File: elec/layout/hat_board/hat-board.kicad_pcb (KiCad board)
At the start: 4 copper layers, 108 x 115.9 mm, 82 parts, among them P1 HatButtonAntenna, U1 _NXP_Semicon_PN5321A3HN_C106_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, U10 _OPSCO_Optoelectronics_SK6805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, U11 _OPSCO_Optoelectronics_SK6805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, U12 _OPSCO_Optoelectronics_SK6805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, U13 _OPSCO_Optoelectronics_SK6805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, U14 _OPSCO_Optoelectronics_SK6805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, U15 _OPSCO_Optoelectronics_SK6805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, U16 _OPSCO_Optoelectronics_SK6805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, U17 _OPSCO_Optoelectronics_SK6805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, U18 _OPSCO_Optoelectronics_SK6805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, U19 _OPSCO_Optoelectronics_SK6805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, U2 _OPSCO_Optoelectronics_SK6805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, U20 _OPSCO_Optoelectronics_SK6805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, U21 _OPSCO_Optoelectronics_SK6805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, U22 _OPSCO_Optoelectronics_SK6805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, U23 _OPSCO_Optoelectronics_SK6805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, U24 _OPSCO_Optoelectronics_SK6805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, U25 _Microchip_Tech_CAP1188_1_CP_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, U3 _OPSCO_Optoelectronics_SK6805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, U4 _OPSCO_Optoelectronics_SK6805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, U5 _OPSCO_Optoelectronics_SK6805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, U6 _OPSCO_Optoelectronics_SK6805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, U7 _OPSCO_Optoelectronics_SK6805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, U8 _OPSCO_Optoelectronics_SK6805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, U9 _OPSCO_Optoelectronics_SK6805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

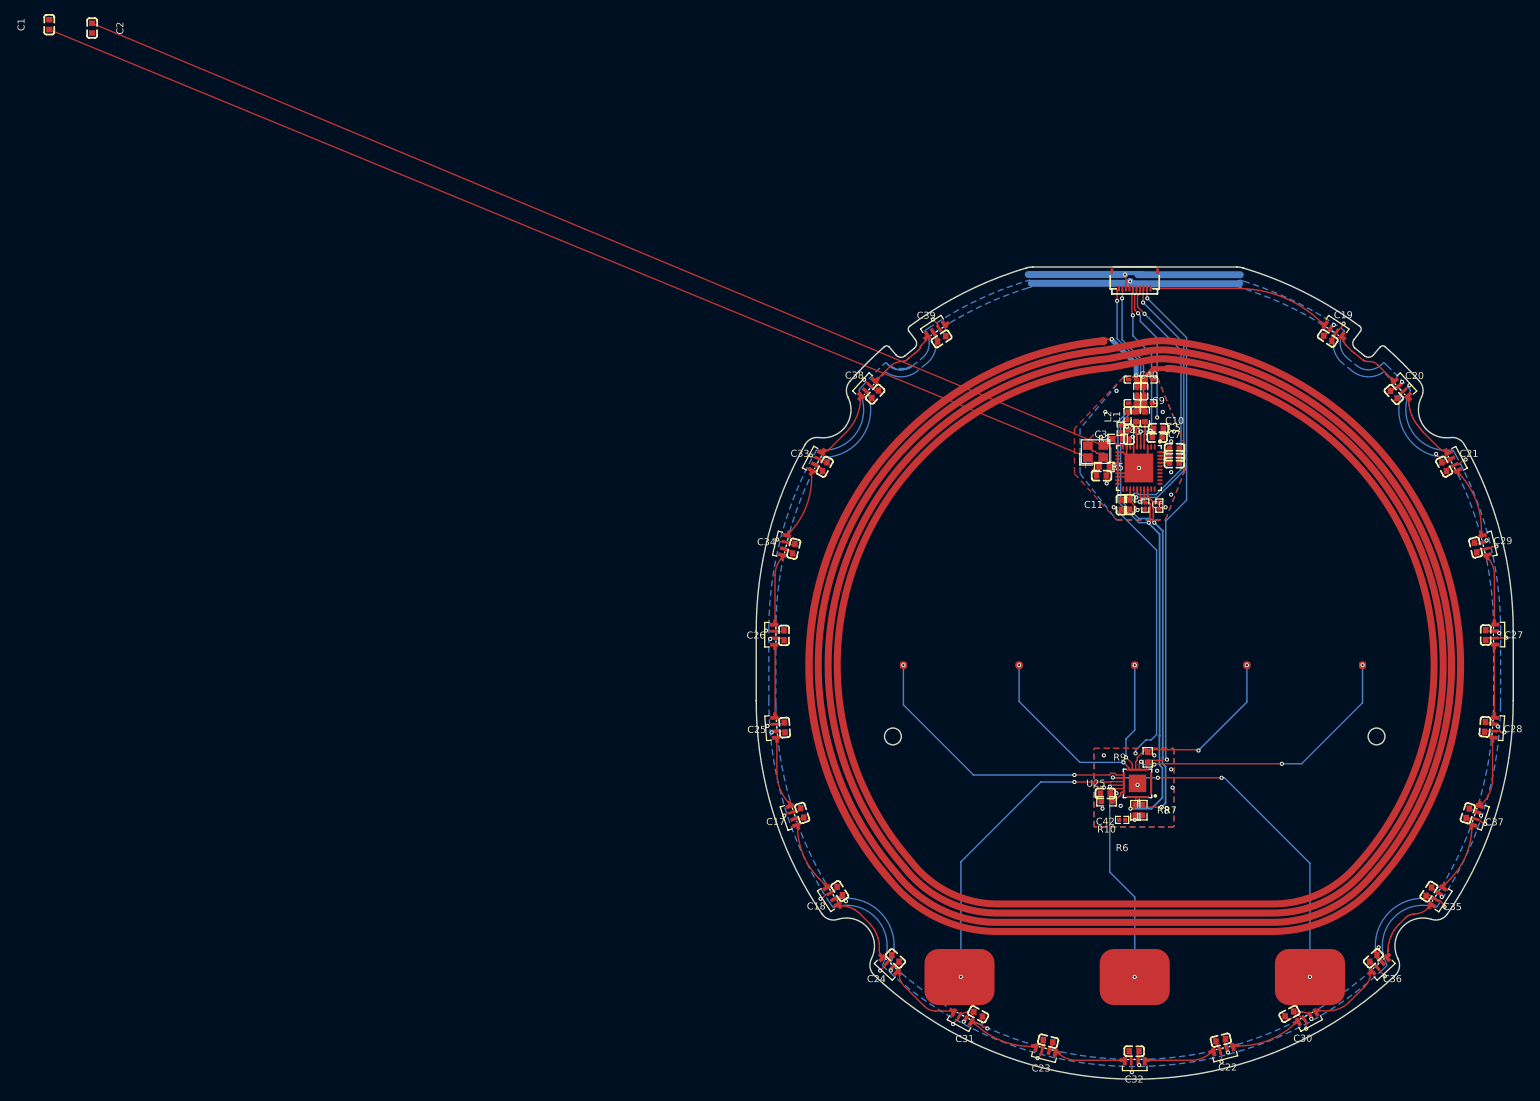
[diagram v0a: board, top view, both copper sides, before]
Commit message: Don't update PCB files
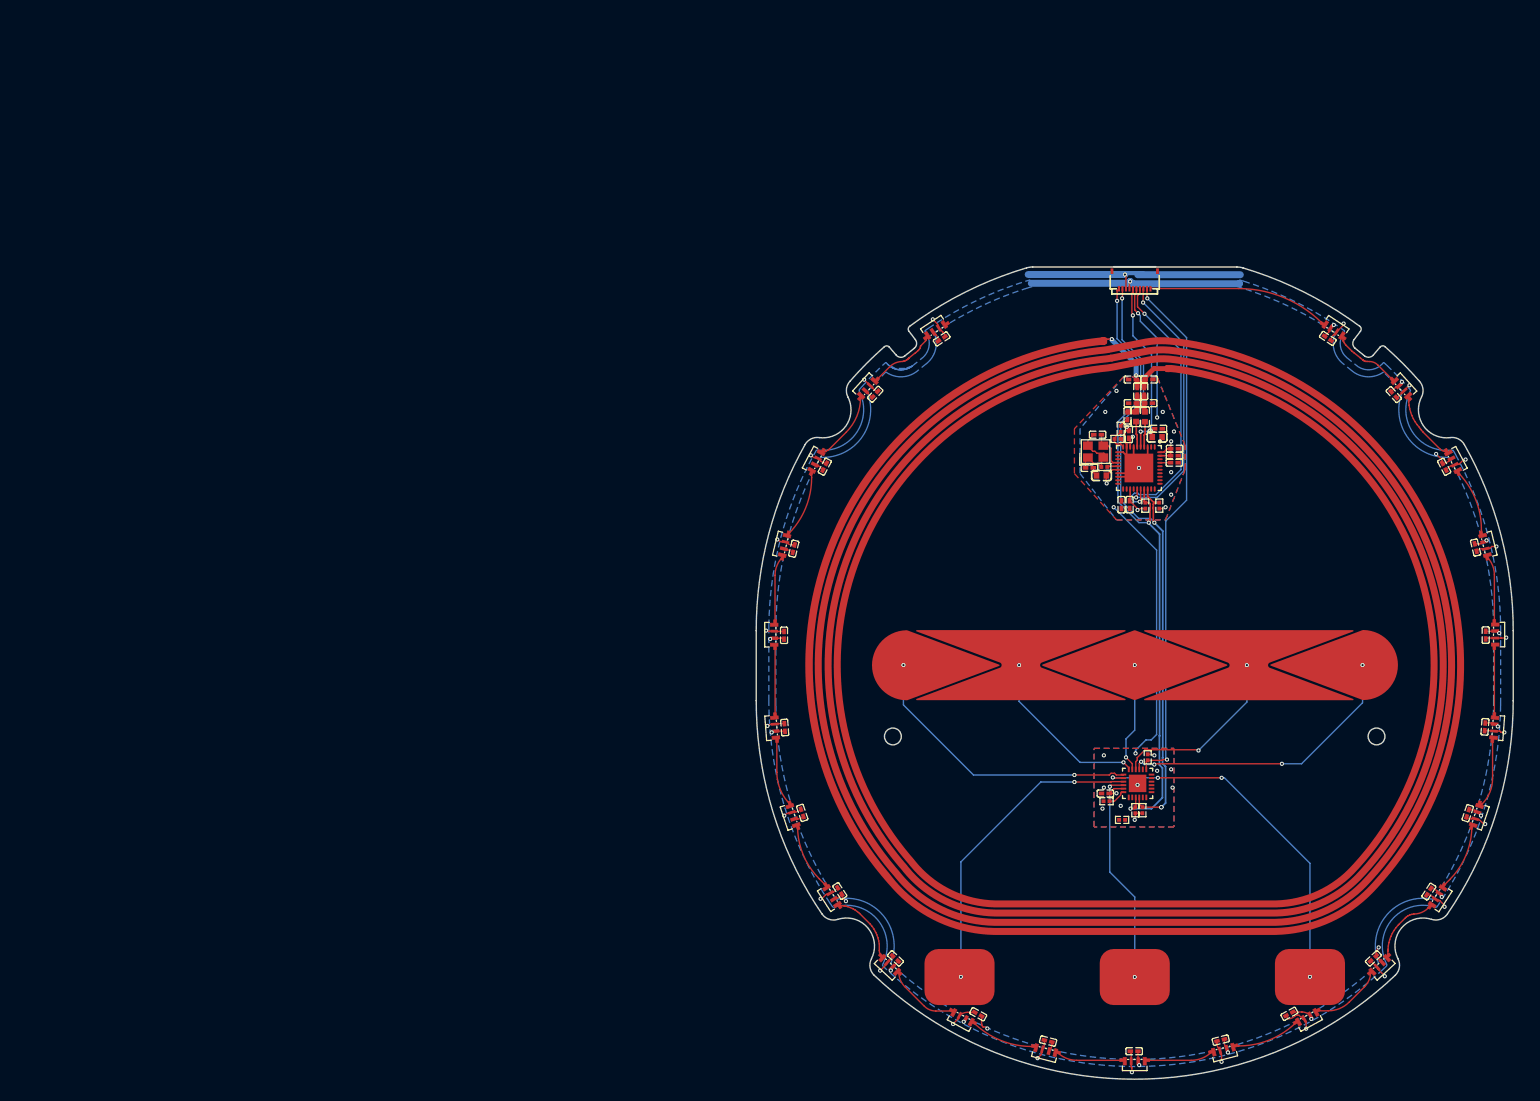
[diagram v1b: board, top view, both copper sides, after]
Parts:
- C1, C2: value 100nF ±10% 50V X7R -> 20pF ±5% 50V C0G; footprint lcsc:C0603 -> lcsc:C0402
- C10, C11, C17, C18, C19, C20, C21, C22, C23, C24, C25, C26, C27, C28, C29, C3, C30, C31, C32, C33, C34, C35, C36, C37, C38, C39, C42, C5, C6, C7, C9: value 100nF ±10% 50V X7R -> 100nF ±10% 16V X7R; footprint lcsc:C0603 -> lcsc:C0402
- C4, C8: value 100nF ±10% 50V X7R -> 10µF ±10% 10V X5R
- L1, L2: value 560nH ±5% infHz 450mA 480mΩ -> 560nH ±5% 450mA 480mΩ
- R1, R2: value 10kΩ ±1% 62.5mW -> 5.1kΩ ±1% 62.5mW
- R10, R9: value 1kΩ ±1% 100mW -> 10kΩ ±1% 62.5mW; footprint lcsc:R0603 -> lcsc:R0402
- R3, R5, R7, R8: value 1kΩ ±1% 100mW -> 5.1kΩ ±1% 62.5mW; footprint lcsc:R0603 -> lcsc:R0402
- U25: footprint lcsc:QFN-24_L4.0-W4.0-P0.50-BL-EP2.5 -> lcsc:QFN-24_L4.0-W4.0-P0.50-TL-EP2.5
- moved C1 161.3 mm to (145.3, 63.0), turned to 0 degrees
- moved C2 154.7 mm to (146.5, 58.2), turned to 180 degrees
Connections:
- C10 pad 1: power_5v -> power_3v3
- C11 pad 1: power_5v -> gnd
- C11 pad 2: gnd -> lv
- C12 pad 2: nfc-net-6 -> nfc-net
- C2 pad 1: nfc-net -> nfc-net-3
- C32 pad 1: power_3v3 -> power_5v
- C33 pad 1: power_3v3 -> power_5v
- C34 pad 1: power_3v3 -> power_5v
- C35 pad 1: power_3v3 -> power_5v
- C36 pad 1: nfc-net-2 -> power_5v
- C37 pad 1: power_3v3 -> power_5v
- C38 pad 1: power_3v3 -> power_5v
- C39 pad 1: power_3v3 -> power_5v
- C4 pad 1: power_5v -> power_3v3
- C42 pad 1: gnd -> power_3v3
- C42 pad 2: lv -> gnd
- C5 pad 1: power_5v -> power_3v3
- C6 pad 1: power_5v -> power_3v3
- C7 pad 1: power_5v -> nfc-net-4
- C8 pad 1: power_5v -> power_3v3
- C9 pad 1: power_5v -> power_3v3
- L1 pad 2: nfc-net-1 -> nfc-net-2
- R1 pad 1: capacitive_sensor-net-1 -> i2c_scl
- R1 pad 2: gnd -> power_3v3
- R10 pad 1: i2c_sda -> capacitive_sensor-net
- R10 pad 2: power_3v3 -> gnd
- R2 pad 1: capacitive_sensor-net -> i2c_sda
- R2 pad 2: gnd -> power_3v3
- R3 pad 2: nfc-net-3 -> nfc-net-6
- R4 pad 1: nfc-net-6 -> nfc-net
- R4 pad 2: nfc-net-4 -> nfc-net-1
- R5 pad 2: nfc-net-4 -> nfc-net-1
- R6 pad 1: touch_irq -> capacitive_sensor.address-signal
- R6 pad 2: power_3v3 -> gnd
- R9 pad 1: i2c_scl -> touch_irq
- U1 pad 10: nfc-net-4 -> nfc-net-1
- U1 pad 14: nfc-net -> nfc-net-3
- U1 pad 15: nfc-net-3 -> nfc-net-6
- U1 pad 20: nfc.nfc_ic.footprint.pins[12].net-net -> nfc.nfc_ic-net
- U1 pad 21: nfc.nfc_ic.footprint.pins[13].net-net -> nfc.nfc_ic-net
- U1 pad 22: nfc.nfc_ic.footprint.pins[14].net-net -> nfc.nfc_ic-net
- U1 pad 37: nfc-net-2 -> nfc-net-4
- U1 pad 4: nfc-net-1 -> nfc-net-2
- U10 pad 1: signal-17 -> signal-1
- U10 pad 4: signal-19 -> signal-16
- U11 pad 1: signal-16 -> signal
- U11 pad 4: signal-17 -> signal-1
- U12 pad 1: signal-21 -> signal-9
- U12 pad 4: signal-16 -> signal
- U13 pad 1: signal-9 -> signal-6
- U13 pad 4: signal-10 -> signal-7
- U14 pad 1: signal-11 -> signal-8
- U14 pad 4: signal-21 -> signal-9
- U15 pad 1: signal -> signal-21
- U15 pad 4: signal-11 -> signal-8
- U16 pad 4: signal -> signal-21
- U17 pad 1: signal-20 -> signal-12
- U17 pad 4: signal-9 -> signal-6
- U18 pad 1: signal-15 -> signal-18
- U18 pad 4: signal-20 -> signal-12
- U19 pad 1: signal-2 -> signal-5
- U19 pad 4: signal-15 -> signal-18
- U2 pad 1: signal-10 -> signal-7
- U20 pad 1: signal-1 -> signal-4
- U20 pad 4: signal-2 -> signal-5
- U21 pad 1: signal-6 -> signal-11
- U21 pad 4: signal-1 -> signal-4
- U22 pad 1: signal-5 -> signal-10
- U22 pad 4: signal-6 -> signal-11
- U23 pad 1: signal-4 -> signal-13
- U23 pad 4: signal-5 -> signal-10
- U24 pad 1: signal-3 -> signal-15
- U24 pad 4: signal-4 -> signal-13
- U25 pad 14: capacitive_sensor-net-1 -> addr_comm
- U3 pad 1: signal-18 -> signal-20
- U3 pad 4: signal-3 -> signal-15
- U4 pad 4: signal-18 -> signal-20
- U5 pad 1: signal-13 -> signal-3
- U6 pad 1: signal-8 -> signal-2
- U6 pad 4: signal-13 -> signal-3
- U7 pad 1: signal-7 -> signal-19
- U7 pad 4: signal-8 -> signal-2
- U8 pad 1: signal-12 -> signal-17
- U8 pad 4: signal-7 -> signal-19
- U9 pad 1: signal-19 -> signal-16
- U9 pad 4: signal-12 -> signal-17
- XTAL1 pad 3: nfc-net -> nfc-net-3
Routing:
- net nfc.oscillator-net: track 166.9 -> 6.65 mm
- net nfc-net: track 157.9 -> 1.57 mm

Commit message: Build full
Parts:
- C1, C2: value 20pF ±5% 50V C0G -> 100nF ±10% 50V X7R; footprint lcsc:C0402 -> lcsc:C0603
- C10, C11, C17, C18, C19, C20, C21, C22, C23, C24, C25, C26, C27, C28, C29, C3, C30, C31, C32, C33, C34, C35, C36, C37, C38, C39, C42, C5, C6, C7, C9: value 100nF ±10% 16V X7R -> 100nF ±10% 50V X7R; footprint lcsc:C0402 -> lcsc:C0603
- C4, C8: value 10µF ±10% 10V X5R -> 100nF ±10% 50V X7R
- L1, L2: value 560nH ±5% 450mA 480mΩ -> 560nH ±5% infHz 450mA 480mΩ
- R1, R2: value 5.1kΩ ±1% 62.5mW -> 10kΩ ±1% 62.5mW
- R10, R9: value 10kΩ ±1% 62.5mW -> 1kΩ ±1% 100mW; footprint lcsc:R0402 -> lcsc:R0603
- R3, R5, R7, R8: value 5.1kΩ ±1% 62.5mW -> 1kΩ ±1% 100mW; footprint lcsc:R0402 -> lcsc:R0603
- U25: footprint lcsc:QFN-24_L4.0-W4.0-P0.50-TL-EP2.5 -> lcsc:QFN-24_L4.0-W4.0-P0.50-BL-EP2.5
- moved C1 161.3 mm to (-3.05, -0.25), turned to 90 degrees
- moved C2 154.7 mm to (3.05, 0.25), turned to 270 degrees
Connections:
- C10 pad 1: power_3v3 -> power_5v
- C11 pad 1: gnd -> power_5v
- C11 pad 2: lv -> gnd
- C12 pad 2: nfc-net -> nfc-net-6
- C2 pad 1: nfc-net-3 -> nfc-net
- C32 pad 1: power_5v -> power_3v3
- C33 pad 1: power_5v -> power_3v3
- C34 pad 1: power_5v -> power_3v3
- C35 pad 1: power_5v -> power_3v3
- C36 pad 1: power_5v -> nfc-net-2
- C37 pad 1: power_5v -> power_3v3
- C38 pad 1: power_5v -> power_3v3
- C39 pad 1: power_5v -> power_3v3
- C4 pad 1: power_3v3 -> power_5v
- C42 pad 1: power_3v3 -> gnd
- C42 pad 2: gnd -> lv
- C5 pad 1: power_3v3 -> power_5v
- C6 pad 1: power_3v3 -> power_5v
- C7 pad 1: nfc-net-4 -> power_5v
- C8 pad 1: power_3v3 -> power_5v
- C9 pad 1: power_3v3 -> power_5v
- L1 pad 2: nfc-net-2 -> nfc-net-1
- R1 pad 1: i2c_scl -> capacitive_sensor-net-1
- R1 pad 2: power_3v3 -> gnd
- R10 pad 1: capacitive_sensor-net -> i2c_sda
- R10 pad 2: gnd -> power_3v3
- R2 pad 1: i2c_sda -> capacitive_sensor-net
- R2 pad 2: power_3v3 -> gnd
- R3 pad 2: nfc-net-6 -> nfc-net-3
- R4 pad 1: nfc-net -> nfc-net-6
- R4 pad 2: nfc-net-1 -> nfc-net-4
- R5 pad 2: nfc-net-1 -> nfc-net-4
- R6 pad 1: capacitive_sensor.address-signal -> touch_irq
- R6 pad 2: gnd -> power_3v3
- R9 pad 1: touch_irq -> i2c_scl
- U1 pad 10: nfc-net-1 -> nfc-net-4
- U1 pad 14: nfc-net-3 -> nfc-net
- U1 pad 15: nfc-net-6 -> nfc-net-3
- U1 pad 20: nfc.nfc_ic-net -> nfc.nfc_ic.footprint.pins[12].net-net
- U1 pad 21: nfc.nfc_ic-net -> nfc.nfc_ic.footprint.pins[13].net-net
- U1 pad 22: nfc.nfc_ic-net -> nfc.nfc_ic.footprint.pins[14].net-net
- U1 pad 37: nfc-net-4 -> nfc-net-2
- U1 pad 4: nfc-net-2 -> nfc-net-1
- U10 pad 1: signal-1 -> signal-17
- U10 pad 4: signal-16 -> signal-19
- U11 pad 1: signal -> signal-16
- U11 pad 4: signal-1 -> signal-17
- U12 pad 1: signal-9 -> signal-21
- U12 pad 4: signal -> signal-16
- U13 pad 1: signal-6 -> signal-9
- U13 pad 4: signal-7 -> signal-10
- U14 pad 1: signal-8 -> signal-11
- U14 pad 4: signal-9 -> signal-21
- U15 pad 1: signal-21 -> signal
- U15 pad 4: signal-8 -> signal-11
- U16 pad 4: signal-21 -> signal
- U17 pad 1: signal-12 -> signal-20
- U17 pad 4: signal-6 -> signal-9
- U18 pad 1: signal-18 -> signal-15
- U18 pad 4: signal-12 -> signal-20
- U19 pad 1: signal-5 -> signal-2
- U19 pad 4: signal-18 -> signal-15
- U2 pad 1: signal-7 -> signal-10
- U20 pad 1: signal-4 -> signal-1
- U20 pad 4: signal-5 -> signal-2
- U21 pad 1: signal-11 -> signal-6
- U21 pad 4: signal-4 -> signal-1
- U22 pad 1: signal-10 -> signal-5
- U22 pad 4: signal-11 -> signal-6
- U23 pad 1: signal-13 -> signal-4
- U23 pad 4: signal-10 -> signal-5
- U24 pad 1: signal-15 -> signal-3
- U24 pad 4: signal-13 -> signal-4
- U25 pad 14: addr_comm -> capacitive_sensor-net-1
- U3 pad 1: signal-20 -> signal-18
- U3 pad 4: signal-15 -> signal-3
- U4 pad 4: signal-20 -> signal-18
- U5 pad 1: signal-3 -> signal-13
- U6 pad 1: signal-2 -> signal-8
- U6 pad 4: signal-3 -> signal-13
- U7 pad 1: signal-19 -> signal-7
- U7 pad 4: signal-2 -> signal-8
- U8 pad 1: signal-17 -> signal-12
- U8 pad 4: signal-19 -> signal-7
- U9 pad 1: signal-16 -> signal-19
- U9 pad 4: signal-17 -> signal-12
- XTAL1 pad 3: nfc-net-3 -> nfc-net
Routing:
- net nfc.oscillator-net: track 6.65 -> 166.9 mm
- net nfc-net: track 1.57 -> 157.9 mm
